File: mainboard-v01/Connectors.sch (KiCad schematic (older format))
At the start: 16 parts, among them J1 503182-1852, J2 10118194-0001LF, J3 DCJ0303, U20 MR25H40MDF

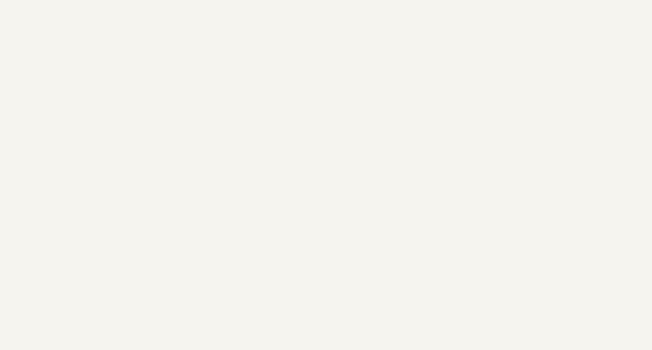
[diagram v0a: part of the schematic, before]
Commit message: adding v01 schematic pdf
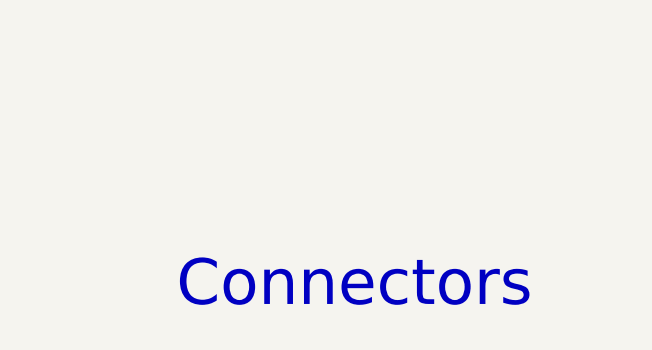
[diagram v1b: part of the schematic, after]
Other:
- note added: "Connectors"
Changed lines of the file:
@@
 	6800 3100 7000 3100
 Connection ~ 7000 3100
+Text Notes 8600 7600 0    200  ~ 0
+Connectors
 $EndSCHEMATC
